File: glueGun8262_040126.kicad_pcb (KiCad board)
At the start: 2 copper layers, 29 parts, among them CN1 KF243-5.0-2P, CN2 KF243-5.0-2P, CN3 KF243-5.0-2P, CN4 KF243-5.0-2P, CN5 KF243-5.0-2P, CN6 KF243-5.0-2P, U1 DRV8262DDWR, U2 DRV8262DDWR, U3 ESP32-S3-DEVKITC-1-N8R2

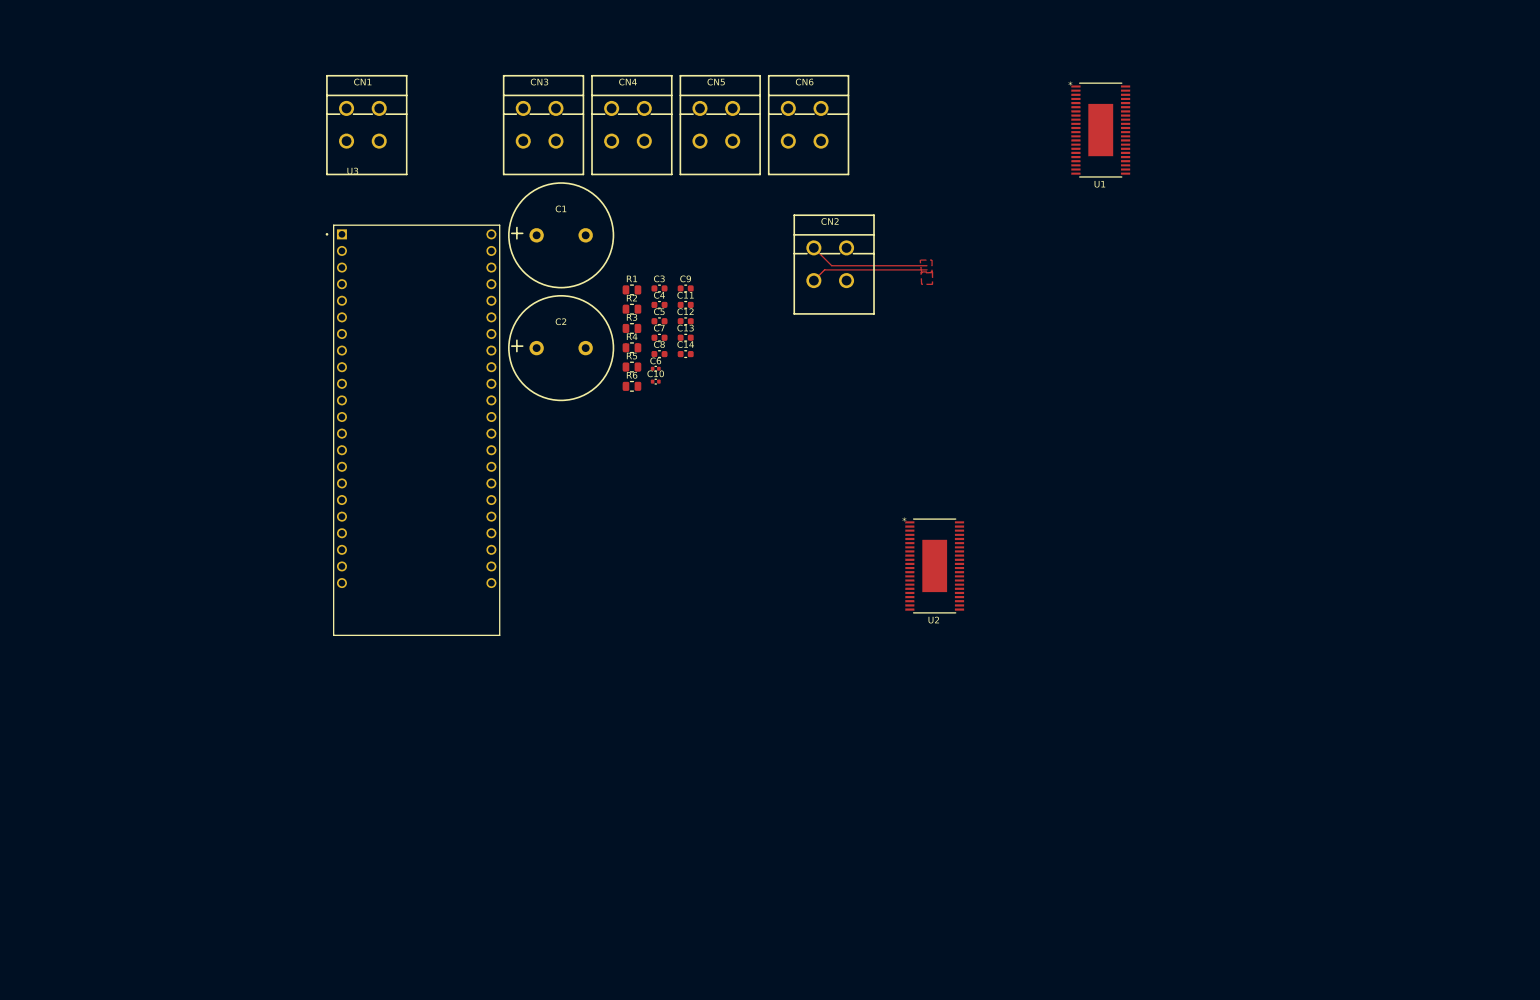
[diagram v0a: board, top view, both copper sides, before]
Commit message: ina240 schunts in series with sol
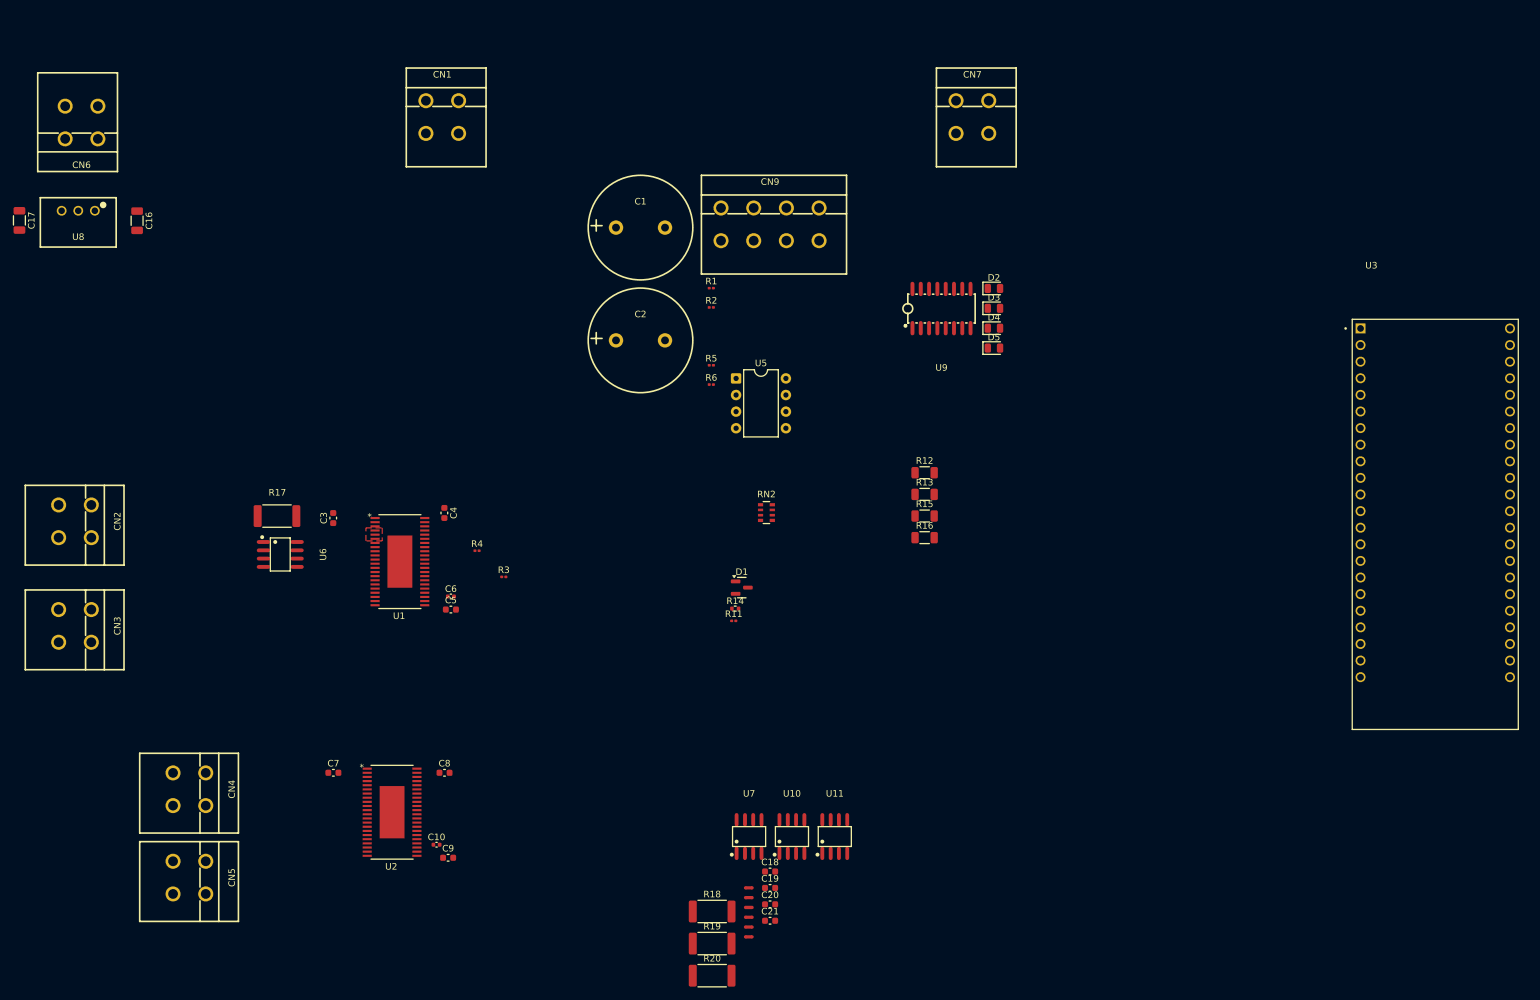
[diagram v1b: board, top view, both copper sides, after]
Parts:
- removed C11, C12, C13, C14: 10nf, Capacitor_SMD:C_0603_1608Metric
- added C16: 10uf 50v, Capacitor_SMD:C_1206_3216Metric, F.Cu at (52.0, 67.5)
- added C17: 22uf 10v, Capacitor_SMD:C_1206_3216Metric, F.Cu at (34.0, 67.5)
- added C18: 100nf, Capacitor_SMD:C_0603_1608Metric, F.Cu at (148.8, 167.1)
- added C19: 100nf, Capacitor_SMD:C_0603_1608Metric, F.Cu at (148.8, 169.6)
- added C20: 100nf, Capacitor_SMD:C_0603_1608Metric, F.Cu at (148.8, 172.1)
- added C21: 100nf, Capacitor_SMD:C_0603_1608Metric, F.Cu at (148.8, 174.6)
- added CN7: KF243-5.0-2P, easyeda2kicad:CONN-TH_P5.00_KF243-5.0-2P, F.Cu at (179.8, 51.7)
- added CN9: KF243-5.0-4P, easyeda2kicad:CONN-TH_4P-P5.00_KF243-5.0-4P, F.Cu at (148.8, 68.1)
- added D1: D_Schottky, Package_TO_SOT_SMD:SOT-23, F.Cu at (144.5, 123.6)
- added D2: green, LED_SMD:LED_0805_2012Metric, F.Cu at (183.1, 77.9)
- added D3: green, LED_SMD:LED_0805_2012Metric, F.Cu at (183.1, 80.9)
- added D4: green, LED_SMD:LED_0805_2012Metric, F.Cu at (183.1, 84.0)
- added D5: green, LED_SMD:LED_0805_2012Metric, F.Cu at (183.1, 87.0)
- added NT1: NetTie_2, NetTie:NetTie-2_SMD_Pad0.5mm, F.Cu at (76.4, 112.7)
- added NT2: NetTie_2, NetTie:NetTie-2_SMD_Pad0.5mm, F.Cu at (70.4, 112.7)
- added NT3: NetTie_2, NetTie:NetTie-2_SMD_Pad0.5mm, F.Cu at (145.6, 169.6)
- added NT4: NetTie_2, NetTie:NetTie-2_SMD_Pad0.5mm, F.Cu at (145.6, 171.1)
- added NT5: NetTie_2, NetTie:NetTie-2_SMD_Pad0.5mm, F.Cu at (145.6, 172.6)
- added NT6: NetTie_2, NetTie:NetTie-2_SMD_Pad0.5mm, F.Cu at (145.6, 174.1)
- added NT7: NetTie_2, NetTie:NetTie-2_SMD_Pad0.5mm, F.Cu at (145.6, 175.6)
- added NT8: NetTie_2, NetTie:NetTie-2_SMD_Pad0.5mm, F.Cu at (145.6, 177.1)
- added R11: 470r, Resistor_SMD:R_0201_0603Metric, F.Cu at (143.3, 128.7)
- added R12: 2.2k, Resistor_SMD:R_1206_3216Metric, F.Cu at (172.5, 106.1)
- added R13: 2.2k, Resistor_SMD:R_1206_3216Metric, F.Cu at (172.5, 109.4)
- added R14: 5.1k, Resistor_SMD:R_0402_1005Metric, F.Cu at (143.5, 126.9)
- added R15: 2.2k, Resistor_SMD:R_1206_3216Metric, F.Cu at (172.5, 112.7)
- added R16: 2.2k, Resistor_SMD:R_1206_3216Metric, F.Cu at (172.5, 116.0)
- added R17: 40m, Resistor_SMD:R_2512_6332Metric, F.Cu at (73.4, 112.7)
- added R18: 40m, Resistor_SMD:R_2512_6332Metric, F.Cu at (140.0, 173.2)
- added R19: 40m, Resistor_SMD:R_2512_6332Metric, F.Cu at (140.0, 178.1)
- added R20: 40m, Resistor_SMD:R_2512_6332Metric, F.Cu at (140.0, 183.0)
- added RN2: 10k, Resistor_SMD:R_Array_Convex_4x0603, F.Cu at (148.3, 112.2)
- added U10: INA240A2DR, easyeda2kicad:SOIC-8_L4.9-W3.9-P1.27-LS6.0-BL, F.Cu at (152.2, 161.7)
- added U11: INA240A2DR, easyeda2kicad:SOIC-8_L4.9-W3.9-P1.27-LS6.0-BL, F.Cu at (158.7, 161.7)
- added U5: 6N137, Package_DIP:DIP-8_W7.62mm, F.Cu at (143.6, 91.6)
- added U6: INA240A2DR, easyeda2kicad:SOIC-8_L4.9-W3.9-P1.27-LS6.0-BL, F.Cu at (73.9, 118.6)
- added U7: INA240A2DR, easyeda2kicad:SOIC-8_L4.9-W3.9-P1.27-LS6.0-BL, F.Cu at (145.6, 161.7)
- added U8: K7805-1000R3_C2992391, easyeda2kicad:PWRM-TH_YLPTEC_K78XX-1000R3, F.Cu at (43.0, 66.0)
- added U9: TLP281-4(GB-TP,J,F, easyeda2kicad:SOP-16_L10.3-W4.4-P1.27-LS7.0-BL, F.Cu at (175.0, 81.0)
- R1, R2: footprint Resistor_SMD:R_0805_2012Metric -> Resistor_SMD:R_0201_0603Metric
- R3, R4, R5, R6: value 13k -> 5k; footprint Resistor_SMD:R_0805_2012Metric -> Resistor_SMD:R_0201_0603Metric
- moved U3 156.5 mm to (250.6, 114.0)
- moved CN5 140.6 mm to (60.0, 168.0), turned to -90 degrees
- moved U1 125.9 mm to (92.2, 119.7)
- moved CN2 122.0 mm to (42.5, 113.5), turned to -90 degrees
- moved CN4 121.8 mm to (60.0, 154.5), turned to -90 degrees
- moved CN6 110.6 mm to (43.5, 52.5), turned to 180 degrees
- moved CN3 104.5 mm to (42.5, 129.5), turned to -90 degrees
- moved C9 94.4 mm to (99.6, 165.0)
- moved U2 91.1 mm to (91.0, 158.0)
- moved C7 83.2 mm to (82.0, 152.0)
- moved C10 78.4 mm to (97.8, 163.0)
- moved C8 72.0 mm to (99.0, 152.0)
- moved C3 61.0 mm to (82.0, 113.0), turned to 90 degrees
- moved C5 54.4 mm to (100.0, 127.0)
- moved C6 46.9 mm to (100.0, 125.0)
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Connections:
- net Net-(CN2-Pad2) renamed /U1_OUT2
- net Net-(CN4-Pad2) renamed /U2_OUT2
- CN3 pad 1: Net-(CN3-Pad1) -> /U1_OUT4
- CN5 pad 1: Net-(CN5-Pad1) -> /U2_OUT4
- CN6 pad 1: unconnected-(CN6-Pad1) -> Net-(U8-VIN)
- CN6 pad 2: unconnected-(CN6-Pad2) -> GND
- U1 pad 10: /U1_PGND12 -> GND
- U1 pad 13: /U1_PGND34 -> GND
- U1 pad 14: Net-(CN3-Pad2) -> /U1_OUT4
- U1 pad 15: Net-(CN3-Pad2) -> /U1_OUT4
- U1 pad 16: Net-(CN3-Pad2) -> /U1_OUT4
- U1 pad 17: Net-(CN3-Pad1) -> /U1_OUT3
- U1 pad 18: Net-(CN3-Pad1) -> /U1_OUT3
- U1 pad 19: Net-(CN3-Pad1) -> /U1_OUT3
- U1 pad 20: /U1_PGND34 -> GND
- U1 pad 3: /U1_PGND12 -> GND
- U1 pad 4: Net-(CN2-Pad1) -> /U1_OUT1
- U1 pad 5: Net-(CN2-Pad1) -> /U1_OUT1
- U1 pad 6: Net-(CN2-Pad1) -> /U1_OUT1
- U2 pad 10: /U2_PGND12 -> GND
- U2 pad 13: /U2_PGND34 -> GND
- U2 pad 14: Net-(CN5-Pad2) -> /U2_OUT4
- U2 pad 15: Net-(CN5-Pad2) -> /U2_OUT4
- U2 pad 16: Net-(CN5-Pad2) -> /U2_OUT4
- U2 pad 17: Net-(CN5-Pad1) -> /U2_OUT3
- U2 pad 18: Net-(CN5-Pad1) -> /U2_OUT3
- U2 pad 19: Net-(CN5-Pad1) -> /U2_OUT3
- U2 pad 20: /U2_PGND34 -> GND
- U2 pad 3: /U2_PGND12 -> GND
- U2 pad 4: Net-(CN4-Pad1) -> /U2_OUT1
- U2 pad 5: Net-(CN4-Pad1) -> /U2_OUT1
- U2 pad 6: Net-(CN4-Pad1) -> /U2_OUT1
- U3 pad J1_13: unconnected-(U3-GPIO3-PadJ1_13) -> /Gun3Vref
- U3 pad J1_16: unconnected-(U3-GPIO10-PadJ1_16) -> /Gun4Vref
- U3 pad J1_21: unconnected-(U3-5V0-PadJ1_21) -> +5V
- U3 pad J3_10: unconnected-(U3-GPIO38-PadJ3_10) -> /Input_1_24v
- U3 pad J3_16: unconnected-(U3-GPIO48-PadJ3_16) -> /Input_4_24v
- U3 pad J3_17: unconnected-(U3-GPIO47-PadJ3_17) -> /Input_3_24v
- U3 pad J3_18: unconnected-(U3-GPIO21-PadJ3_18) -> /Input_0_5v
- U3 pad J3_4: unconnected-(U3-GPIO1-PadJ3_4) -> /Gun1Vref
- U3 pad J3_5: unconnected-(U3-GPIO2-PadJ3_5) -> /Gun2Vref
- U3 pad J3_9: unconnected-(U3-MTCK/GPIO39-PadJ3_9) -> /Input_2_24v
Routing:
- net Net-(CN2-Pad1): track 36.4 -> 0.00 mm
- added copper zone on F.Cu, net /U1_OUT1
- removed copper zone on F.Cu, net /U1_OUT2
- removed copper zone on F.Cu, net Net-(CN2-Pad1)

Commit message: satrted laying pcb
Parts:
- removed NT1, NT2, NT3, NT4, NT5, NT6, NT7, NT8: NetTie_2, NetTie:NetTie-2_SMD_Pad0.5mm
- moved C17 221.2 mm to (252.9, 99.3), turned to 0 degrees
- moved C16 202.9 mm to (252.9, 95.9), turned to 0 degrees
- moved CN6 201.0 mm to (244.2, 43.4), turned to 0 degrees
- moved U8 188.5 mm to (230.8, 82.4), turned to 0 degrees
- moved C10 176.2 mm to (261.3, 97.2)
- moved C6 164.0 mm to (261.3, 95.3)
- moved C9 152.6 mm to (230.3, 86.3)
- moved C8 138.9 mm to (226.3, 96.4)
- moved C5 131.3 mm to (226.3, 91.3)
- moved R4 130.8 mm to (233.6, 100.4)
- moved C4 129.5 mm to (226.3, 88.8), turned to 0 degrees
- moved R3 127.6 mm to (233.6, 98.6)
- moved R14 116.8 mm to (257.1, 100.0)
- moved C18 113.0 mm to (230.3, 88.8)
- moved C19 113.0 mm to (230.3, 91.3)
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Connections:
- CN2 pad 1: Net-(CN2-Pad1) -> Net-(U6-IN-)
- CN3 pad 2: Net-(CN3-Pad2) -> Net-(U7-IN-)
- CN4 pad 1: Net-(CN4-Pad1) -> Net-(U10-IN-)
- CN5 pad 2: Net-(CN5-Pad2) -> Net-(U11-IN-)
- R17 pad 1: Net-(CN2-Pad1) -> Net-(U6-IN-)
- R18 pad 1: Net-(CN3-Pad2) -> Net-(U7-IN-)
- R19 pad 1: Net-(CN4-Pad1) -> Net-(U10-IN-)
- R20 pad 1: Net-(CN5-Pad2) -> Net-(U11-IN-)
- U10 pad 8: Net-(U10-IN+) -> /U2_OUT1
- U11 pad 8: Net-(U11-IN+) -> /U2_OUT3
- U6 pad 8: Net-(U6-IN+) -> /U1_OUT1
- U7 pad 8: Net-(U7-IN+) -> /U1_OUT3
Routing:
- net +48V: track 0.00 -> 277.0 mm
- net /U2_OUT2: track 0.00 -> 29.9 mm
- net /U1_OUT4: track 0.00 -> 28.9 mm
- net /U2_OUT4: track 0.00 -> 28.0 mm
- net /U1_OUT2: track 0.00 -> 28.0 mm
- net Net-(U10-IN-): track 0.00 -> 26.4 mm
- net Net-(U7-IN-): track 0.00 -> 21.6 mm
- net Net-(U6-IN-): track 0.00 -> 21.4 mm
- net /U1_OUT1: track 0.00 -> 21.0 mm
- net Net-(U11-IN-): track 0.00 -> 20.2 mm
- net /U2_OUT1: track 0.00 -> 18.3 mm
- net /U2_OUT3: track 0.00 -> 15.4 mm
- net /U1_OUT3: track 0.00 -> 14.8 mm
- net Net-(U1-VCP/GND): track 0.00 -> 1.34 mm
- net Net-(U2-VCP/GND): track 0.00 -> 1.17 mm
- added copper zone on F.Cu, net +48V
- added copper zone on F.Cu, net /U1_OUT2
- added copper zone on F.Cu, net /U1_OUT3
- added copper zone on F.Cu, net /U1_OUT4
- added copper zone on F.Cu, net /U2_OUT1
- added copper zone on F.Cu, net /U2_OUT2
- added copper zone on F.Cu, net /U2_OUT3
- added copper zone on F.Cu, net /U2_OUT4

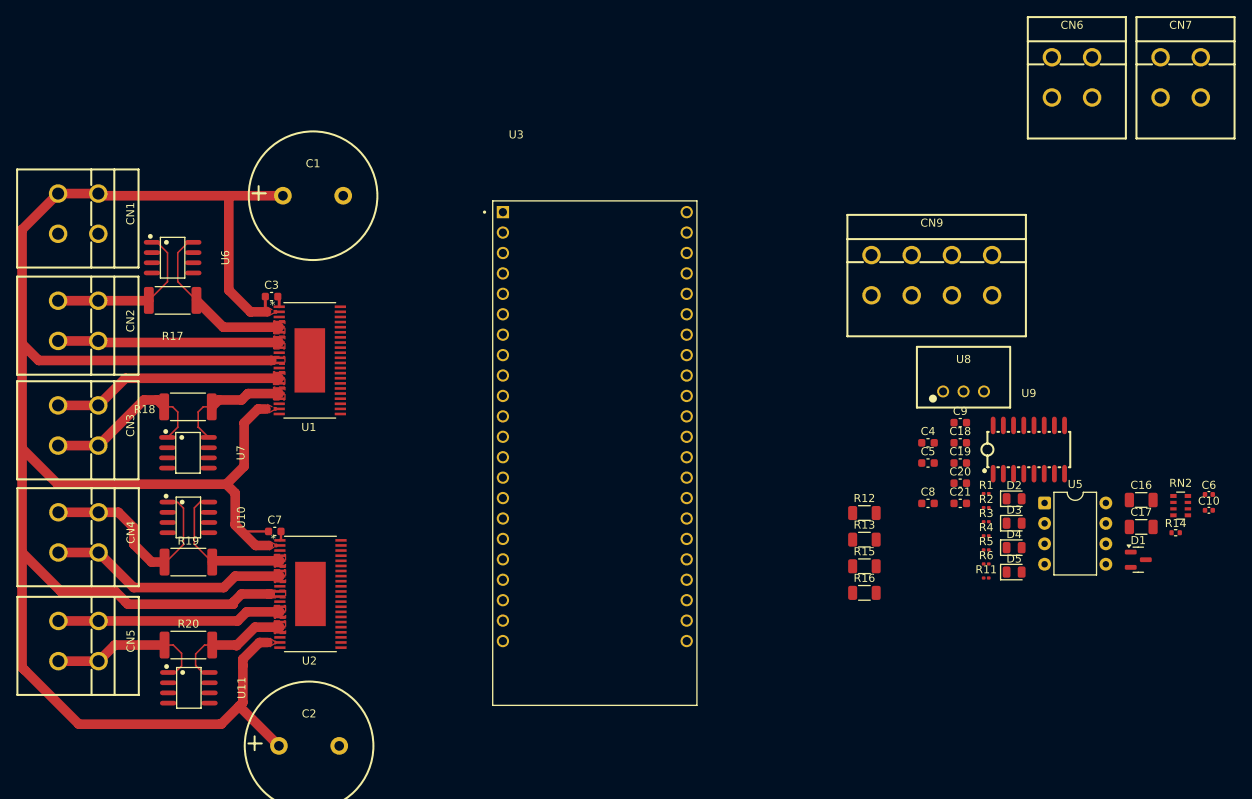
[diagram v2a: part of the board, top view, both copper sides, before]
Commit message: cont arranging board. and easyeda models now in project folder
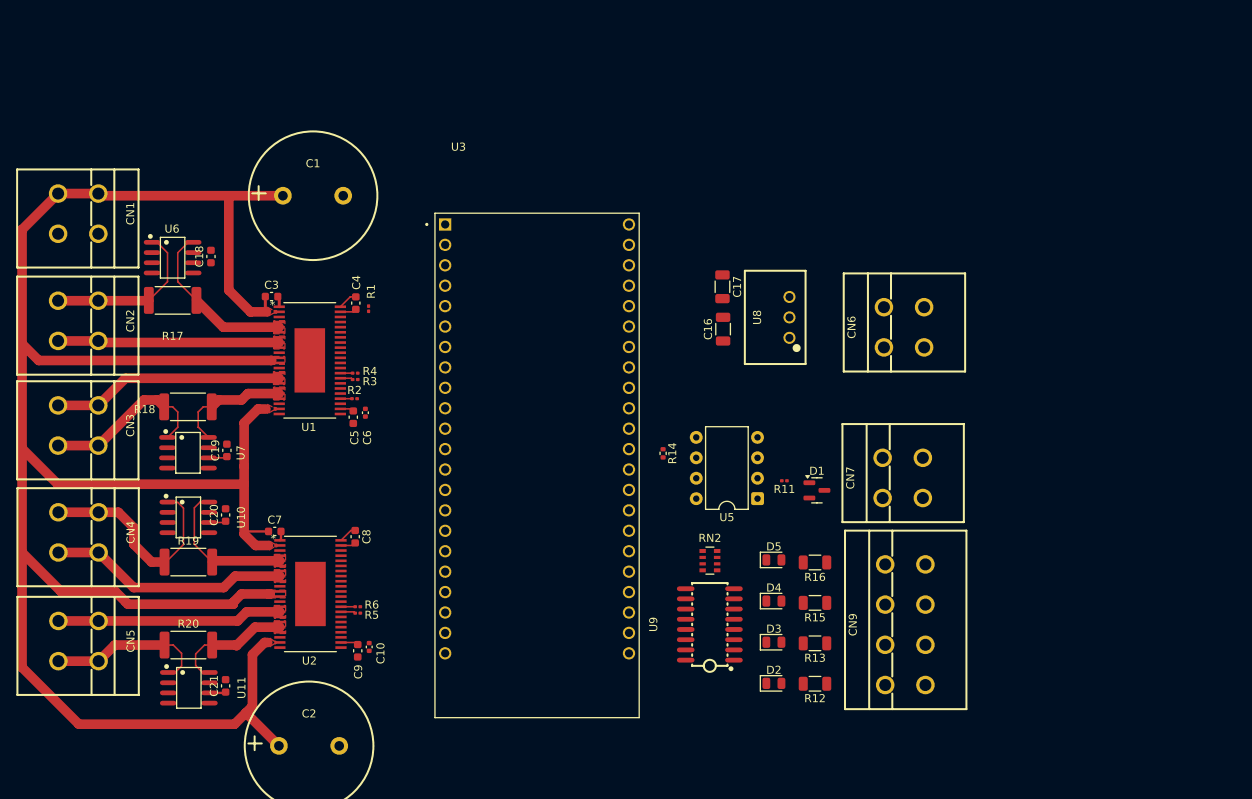
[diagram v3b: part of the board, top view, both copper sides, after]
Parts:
- moved C10 105.8 mm to (156.8, 114.2), turned to -90 degrees
- moved C6 105.4 mm to (156.4, 85.1), turned to -90 degrees
- moved C18 96.0 mm to (137.2, 65.7), turned to 90 degrees
- moved C21 94.1 mm to (139.0, 119.1), turned to 90 degrees
- moved C20 91.4 mm to (139.0, 97.8), turned to 90 degrees
- moved C19 91.2 mm to (139.1, 89.8), turned to 90 degrees
- moved R4 81.0 mm to (155.1, 80.2)
- moved R3 80.4 mm to (155.1, 81.0)
- moved R1 80.2 mm to (156.8, 72.2), turned to 90 degrees
- moved C9 80.1 mm to (155.4, 114.7), turned to -90 degrees
- moved R2 79.7 mm to (155.0, 83.3)
- moved R5 78.6 mm to (155.4, 110.0)
- moved R6 78.3 mm to (155.4, 109.2)
- moved C4 73.3 mm to (155.2, 71.5), turned to -90 degrees
- moved C5 71.7 mm to (154.9, 85.6), turned to -90 degrees
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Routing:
- net +3V3: track 0.00 -> 6.51 mm
- net Net-(U1-CPH/GND): track 0.00 -> 2.43 mm
- net Net-(U2-CPH/GND): track 0.00 -> 2.27 mm
- net Net-(U2-DVDD/CPL): track 0.00 -> 2.19 mm
- net Net-(U1-CPL/DVDD): track 0.00 -> 2.08 mm
- net Net-(U2-CPL/DVDD): track 0.00 -> 1.90 mm
- net Net-(U2-IPROPI/DECAY): track 0.00 -> 1.83 mm
- net Net-(U2-IPROPI/RSVD): track 0.00 -> 1.76 mm
- net Net-(U1-DVDD/CPL): track 0.00 -> 1.71 mm
- net Net-(U1-IPROPI/DECAY): track 0.00 -> 1.59 mm
- net Net-(U1-IPROPI/RSVD): track 0.00 -> 1.53 mm
- net +48V: track 277.0 -> 275.5 mm
- net /nFAULT: track 0.00 -> 1.45 mm
